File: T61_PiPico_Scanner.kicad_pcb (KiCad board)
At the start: 2 copper layers, 60 x 45 mm, 36 parts, among them J101 GND, J102 VBUS, J103 EXT5V, J105 GND, J106 PWRSWITCH, J107 AA01B-S040VA1, Q101 2N7002, Q102 2N7002, Q103 DMG2305UX, U101 Pico

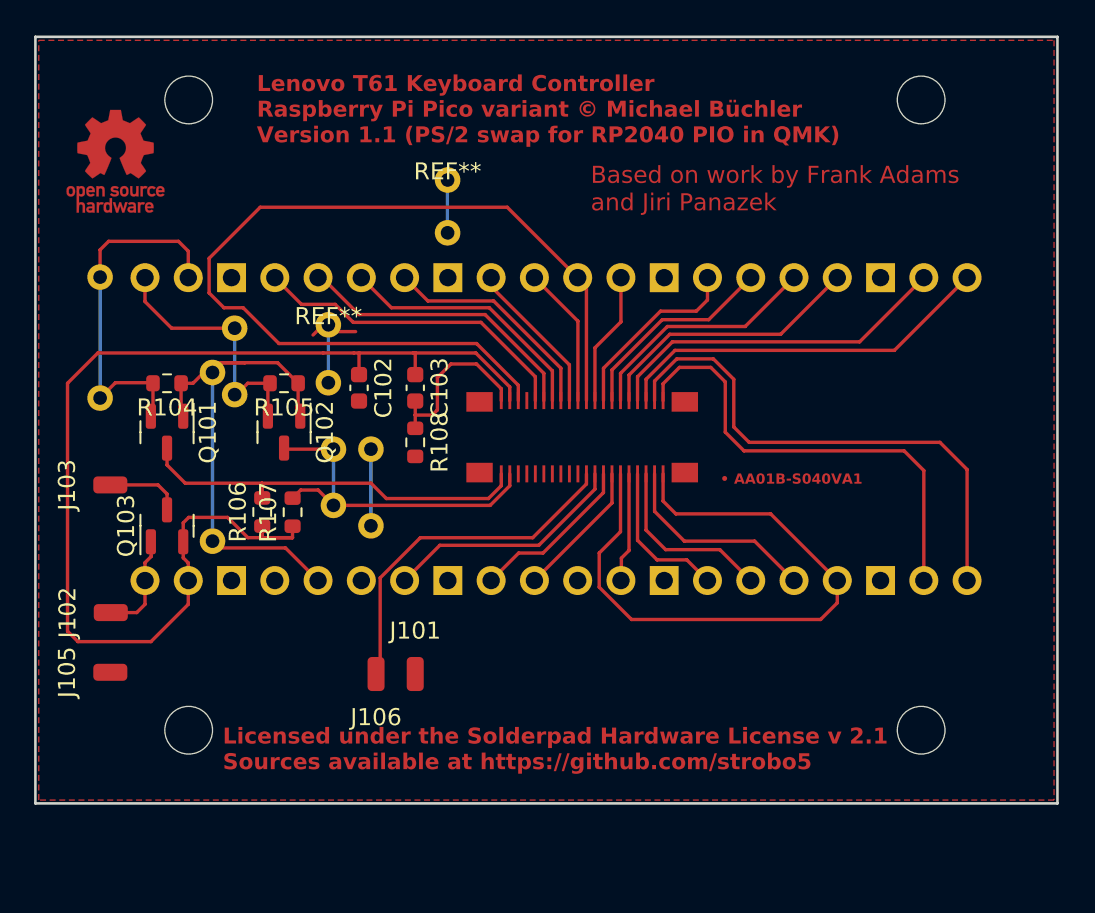
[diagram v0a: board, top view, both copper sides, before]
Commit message: version 1.2: reset IC; Molex 54363-0489
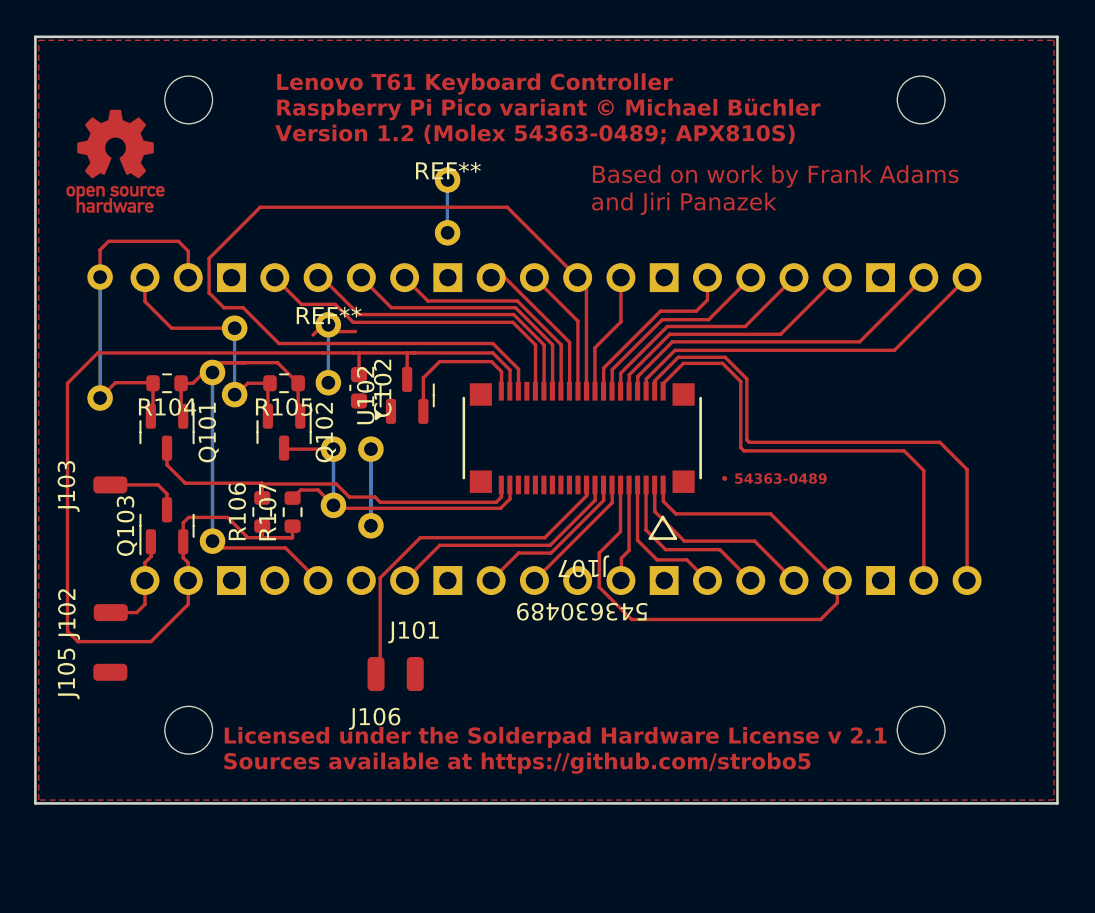
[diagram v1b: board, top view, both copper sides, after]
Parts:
- removed C103: 2u2, Capacitor_SMD:C_0603_1608Metric
- removed R108: 22k, Resistor_SMD:R_0603_1608Metric
- added U102: APX810S-44SR-7, Package_TO_SOT_SMD:SOT-23, F.Cu at (139.8, 104.3)
- J107: value AA01B-S040VA1 -> 54363-0489; footprint T61_Kb_Scanner:AA01B-S040VA1 -> Molex_54363-0489:CON_543630489_var
- moved J107 0.05 mm to (150.1, 106.9), turned to 180 degrees
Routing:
- net /TP4_RESET: track 10.3 -> 8.34 mm
- net /HOTKEY: track 37.4 -> 36.1 mm
- net /SENSE5: track 12.1 -> 11.4 mm
- net /SENSE3: track 8.98 -> 8.34 mm
- net /SENSE2: track 6.46 -> 5.82 mm
- net /SENSE1: track 8.15 -> 7.51 mm
- net /SENSE0: track 10.7 -> 10.0 mm
- net /DRV10: track 11.0 -> 10.4 mm
- net /DRV7: track 14.1 -> 13.6 mm
- net /DRV6: track 20.6 -> 20.1 mm
- net /DRV2: track 12.2 -> 11.6 mm
- net /DRV8: track 22.6 -> 22.0 mm
- net /DRV3: track 16.1 -> 15.5 mm
- net /DRV13: track 19.1 -> 19.7 mm
- net /DRV1: track 7.85 -> 7.30 mm
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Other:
- board text added: "Lenovo T61 Keyboard Controller Raspberry Pi Pico variant © Michael Büchler Version 1.2 (Molex 54363-0489; APX810S)"
- board text added: "• 54363-0489"
- board text removed: "Lenovo T61 Keyboard Controller Raspberry Pi Pico variant © Michael Büchler Version 1.1 (PS/2 swap for RP2040 PIO in QMK)"
- board text removed: "• AA01B-S040VA1"

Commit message: version 2.0: use SMT version of Pi Pico
Now use two layers to allow keyboard connector and Pi Pico to both be on
the top side.

Mechanically incompatible (connector position / mounting holes) but
electrically identical to version 1, i.e. the (QMK) firmware can stay
the same.
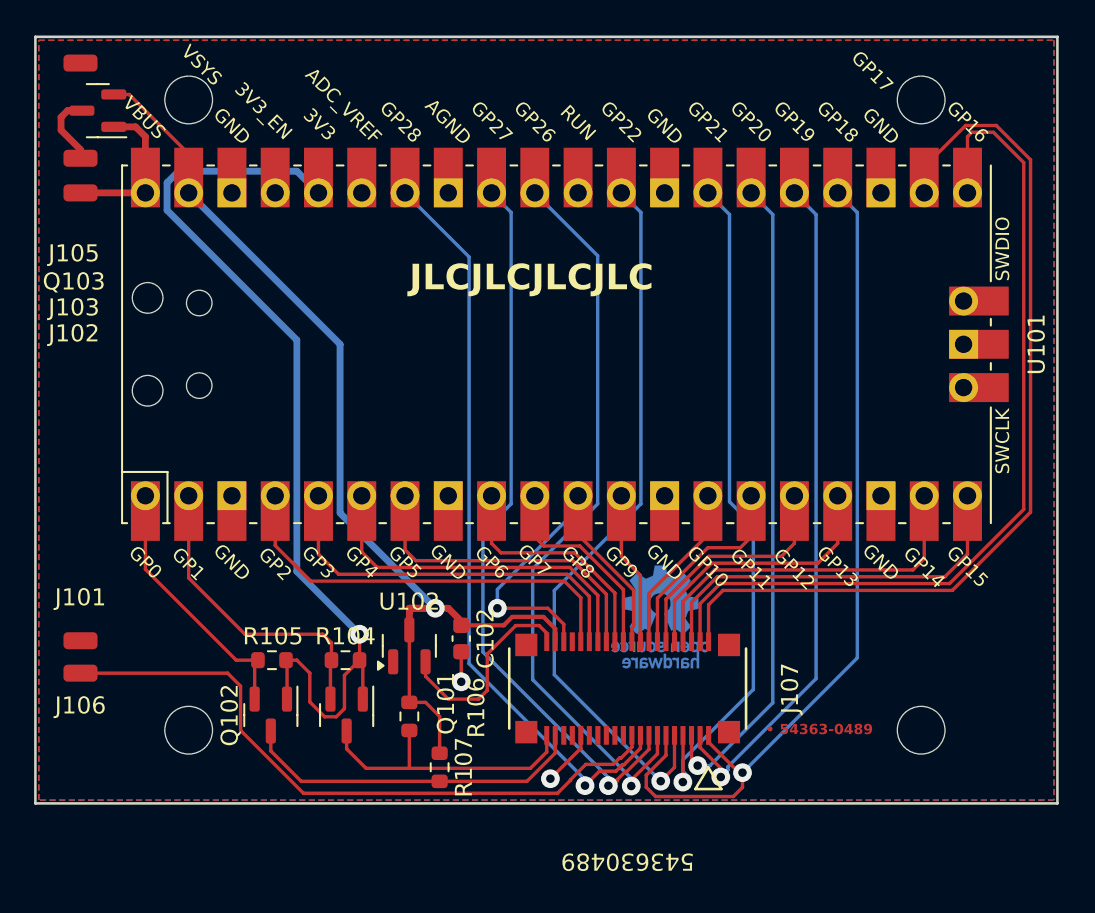
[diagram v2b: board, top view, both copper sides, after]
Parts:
- removed ? (x12): , 
- removed REF** (x2): Pad_TH_as_via, my_footprints:Pad_TH_as_via
- GOLD_ORB_SM101: moved to B.Cu
- U101: footprint T61_Kb_Scanner:RPi_Pico_H -> MCU_RaspberryPi_and_Boards:RPi_Pico_SMD_TH; moved to F.Cu
- moved GOLD_ORB_SM101 41.7 mm to (154.7, 117.3), turned to 180 degrees
- moved J105 35.8 mm to (120.7, 84.8)
- moved Q103 24.7 mm to (121.7, 87.6), turned to 180 degrees
- moved J102 24.7 mm to (120.7, 92.5)
- moved J101 19.7 mm to (120.7, 118.7), turned to -90 degrees
- moved Q101 19.7 mm to (136.3, 123.1)
- moved R104 19.3 mm to (136.2, 119.9)
- moved J103 19.3 mm to (120.7, 90.4)
- moved J106 17.4 mm to (120.7, 120.7), turned to -90 degrees
- moved R107 17.3 mm to (141.7, 126.2), turned to -90 degrees
- moved Q102 16.6 mm to (131.8, 123.1)
- moved R105 16.3 mm to (131.9, 119.9)
- moved C102 15.9 mm to (143.0, 118.6)
- moved J107 14.9 mm to (152.8, 121.6)
- moved R106 14.8 mm to (140.0, 123.2), turned to -90 degrees
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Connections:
- J107 pad 41: GND -> unconnected-(J107-Pad41)
- J107 pad 42: GND -> unconnected-(J107-Pad42)
- J107 pad 43: GND -> unconnected-(J107-Pad43)
- J107 pad 44: GND -> unconnected-(J107-Pad44)
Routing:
- net /SENSE2: track 5.82 -> 42.7 mm, vias 0 -> 1
- net /SENSE1: track 7.51 -> 43.9 mm, vias 0 -> 1
- net /SENSE6: track 9.47 -> 43.2 mm, vias 0 -> 1
- net /SENSE3: track 8.34 -> 40.4 mm, vias 0 -> 1
- net /DRV9: track 54.8 -> 23.8 mm, vias 0 -> 1
- net /SENSE7: track 14.0 -> 44.1 mm, vias 0 -> 1
- net /SENSE5: track 11.4 -> 40.1 mm, vias 0 -> 1
- net /SENSE0: track 10.0 -> 38.3 mm, vias 0 -> 1
- net +3V3: track 30.4 -> 56.3 mm, vias 0 -> 1
- net /DRV4: track 27.6 -> 51.9 mm
- net /DRV5: track 30.9 -> 49.2 mm
- net /PWRSWITCH: track 20.5 -> 38.6 mm
- net /HOTKEY: track 36.1 -> 50.9 mm, vias 0 -> 1
- net +5V: track 69.1 -> 60.2 mm, vias 0 -> 1
- net GND: track 13.6 -> 5.05 mm, vias 0 -> 2
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- added copper zone on B.Cu, net GND
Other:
- board text added: "JLCJLCJLCJLC"
- board text added: "Lenovo T61 Keyboard Controller Raspberry Pi Pico variant © Michael Büchler Version 2.0 (all on top layer)"
- board text removed: "Lenovo T61 Keyboard Controller Raspberry Pi Pico variant © Michael Büchler Version 1.2 (Molex 54363-0489; APX810S)"
